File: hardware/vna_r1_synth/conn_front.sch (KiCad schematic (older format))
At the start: 5 parts

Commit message: work on vna r1 synth schematic
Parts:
- added C? (x5): C_Small, symbol C_Small
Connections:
- net AUX_OUT: now also C?.2; no longer U?.1 (RF)
- net LO_1: now also C?.2; no longer U?.1 (RF)
- net LO_2: now also C?.2; no longer U?.1 (RF)
- net PORT_1: now also C?.2; no longer U?.1 (RF)
- net PORT_2: now also C?.2; no longer U?.1 (RF)
- new net: C?.1, U?.1 (RF) (x5)
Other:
- note removed: "PORTS 1 and 2 are DC coupled to 0V"
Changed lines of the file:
@@
 Comment4 ""
 $EndDescr
-Text HLabel 5450 1600 0    60   Input ~ 0
+Text HLabel 4900 1600 0    60   Input ~ 0
 PORT_1
-Text HLabel 5450 2700 0    60   Input ~ 0
+Text HLabel 4900 2700 0    60   Input ~ 0
 PORT_2
-Text HLabel 5500 4100 0    60   Input ~ 0
+Text HLabel 4950 4100 0    60   Input ~ 0
 LO_1
-Text HLabel 5500 6500 0    60   Input ~ 0
+Text HLabel 4950 6500 0    60   Input ~ 0
 LO_2
-Text HLabel 5500 5200 0    60   Input ~ 0
+Text HLabel 4950 5200 0    60   Input ~ 0
 AUX_OUT
 $Comp
@@
 	1    0    0    -1
 $EndComp
-Wire Wire Line
-	6000 2050 6000 2100
-Wire Wire Line
-	6000 2100 6100 2100
-Wire Wire Line
-	6100 2100 6100 2050
-Wire Wire Line
-	6050 2100 6050 2150
-Connection ~ 6050 2100
-Wire Wire Line
-	5450 1600 5650 1600
 $Comp
 L CONN_SMA_2GND U?
@@
 	1    0    0    -1
 $EndComp
-Wire Wire Line
-	6000 3150 6000 3200
-Wire Wire Line
-	6000 3200 6100 3200
-Wire Wire Line
-	6100 3200 6100 3150
-Wire Wire Line
-	6050 3200 6050 3250
-Connection ~ 6050 3200
-Wire Wire Line
-	5450 2700 5650 2700
 $Comp
 L CONN_SMA_2GND U?
@@
 	1    0    0    -1
 $EndComp
-Wire Wire Line
-	6050 4550 6050 4600
-Wire Wire Line
-	6050 4600 6150 4600
-Wire Wire Line
-	6150 4600 6150 4550
-Wire Wire Line
-	6100 4600 6100 4650
-Connection ~ 6100 4600
-Wire Wire Line
-	5500 4100 5700 4100
 $Comp
 L CONN_SMA_2GND U?
@@
 	1    0    0    -1
 $EndComp
-Wire Wire Line
-	6050 5650 6050 5700
-Wire Wire Line
-	6050 5700 6150 5700
-Wire Wire Line
-	6150 5700 6150 5650
-Wire Wire Line
-	6100 5700 6100 5750
-Connection ~ 6100 5700
-Wire Wire Line
-	5500 5200 5700 5200
 $Comp
 L CONN_SMA_2GND U?
@@
 	1    0    0    -1
 $EndComp
+$Comp
+L C_Small C?
+U 1 1 5AC32053
+P 5200 4100
+F 0 "C?" H 5210 4170 50  0000 L CNN
+F 1 "C_Small" H 5210 4020 50  0000 L CNN
+F 2 "" H 5200 4100 50  0001 C CNN
+F 3 "" H 5200 4100 50  0001 C CNN
+	1    5200 4100
+	0    1    1    0
+$EndComp
+$Comp
+L C_Small C?
+U 1 1 5AC32137
+P 5200 5200
+F 0 "C?" H 5210 5270 50  0000 L CNN
+F 1 "C_Small" H 5210 5120 50  0000 L CNN
+F 2 "" H 5200 5200 50  0001 C CNN
+F 3 "" H 5200 5200 50  0001 C CNN
+	1    5200 5200
+	0    1    1    0
+$EndComp
+$Comp
+L C_Small C?
+U 1 1 5AC32269
+P 5200 6500
+F 0 "C?" H 5210 6570 50  0000 L CNN
+F 1 "C_Small" H 5210 6420 50  0000 L CNN
+F 2 "" H 5200 6500 50  0001 C CNN
+F 3 "" H 5200 6500 50  0001 C CNN
+	1    5200 6500
+	0    1    1    0
+$EndComp
+Wire Wire Line
+	6000 2050 6000 2100
+Wire Wire Line
+	6000 2100 6100 2100
+Wire Wire Line
+	6100 2100 6100 2050
+Wire Wire Line
+	6050 2100 6050 2150
+Connection ~ 6050 2100
+Wire Wire Line
+	5300 1600 5650 1600
+Wire Wire Line
+	6000 3150 6000 3200
+Wire Wire Line
+	6000 3200 6100 3200
+Wire Wire Line
+	6100 3200 6100 3150
+Wire Wire Line
+	6050 3200 6050 3250
+Connection ~ 6050 3200
+Wire Wire Line
+	5300 2700 5650 2700
+Wire Wire Line
+	6050 4550 6050 4600
+Wire Wire Line
+	6050 4600 6150 4600
+Wire Wire Line
+	6150 4600 6150 4550
+Wire Wire Line
+	6100 4600 6100 4650
+Connection ~ 6100 4600
+Wire Wire Line
+	5300 4100 5700 4100
+Wire Wire Line
+	6050 5650 6050 5700
+Wire Wire Line
+	6050 5700 6150 5700
+Wire Wire Line
+	6150 5700 6150 5650
+Wire Wire Line
+	6100 5700 6100 5750
+Connection ~ 6100 5700
+Wire Wire Line
+	5300 5200 5700 5200
 Wire Wire Line
 	6050 6950 6050 7000
@@
 Connection ~ 6100 7000
 Wire Wire Line
-	5500 6500 5700 6500
-Text Notes 4700 1100 0    60   ~ 0
-PORTS 1 and 2 are DC coupled to 0V
+	5300 6500 5700 6500
+Wire Wire Line
+	4900 1600 5100 1600
+Wire Wire Line
+	5100 2700 4900 2700
+Wire Wire Line
+	4950 4100 5100 4100
+Wire Wire Line
+	5100 5200 4950 5200
+Wire Wire Line
+	5100 6500 4950 6500
+$Comp
+L C_Small C?
+U 1 1 5AC31626
+P 5200 2700
+F 0 "C?" H 5210 2770 50  0000 L CNN
+F 1 "C_Small" H 5210 2620 50  0000 L CNN
+F 2 "" H 5200 2700 50  0001 C CNN
+F 3 "" H 5200 2700 50  0001 C CNN
+	1    5200 2700
+	0    1    1    0
+$EndComp
+$Comp
+L C_Small C?
+U 1 1 5AC31536
+P 5200 1600
+F 0 "C?" H 5210 1670 50  0000 L CNN
+F 1 "C_Small" H 5210 1520 50  0000 L CNN
+F 2 "" H 5200 1600 50  0001 C CNN
+F 3 "" H 5200 1600 50  0001 C CNN
+	1    5200 1600
+	0    1    1    0
+$EndComp
 $EndSCHEMATC

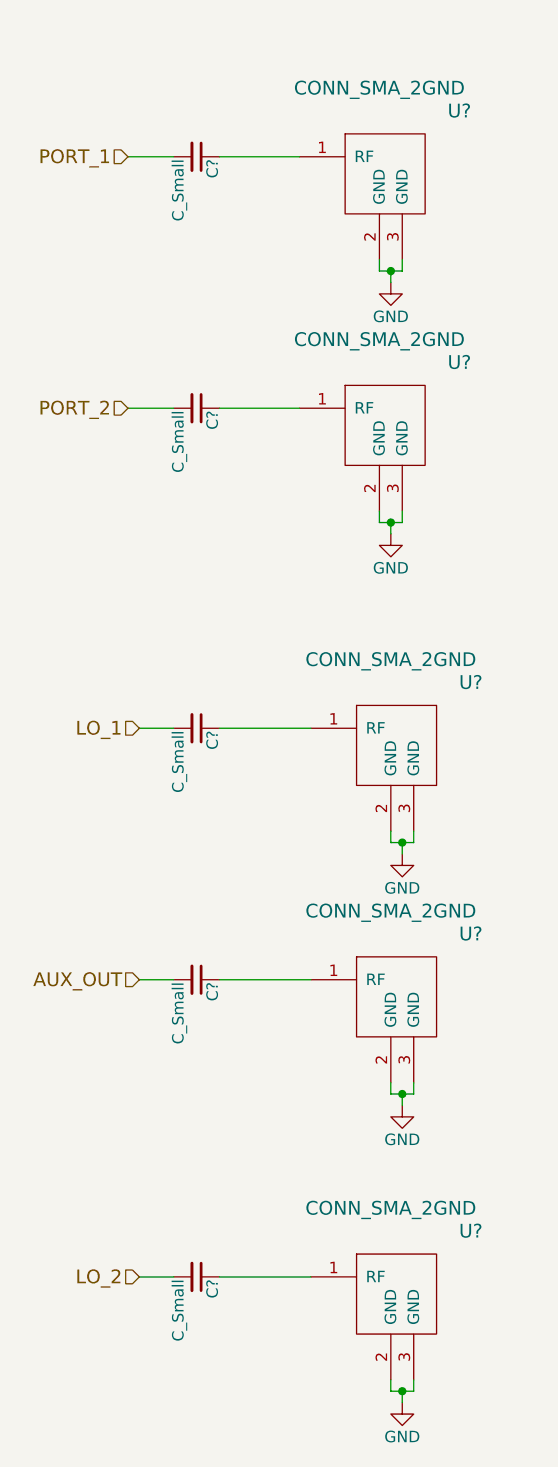
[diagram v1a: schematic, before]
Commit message: footprint assignment for vna r1 synth and demod
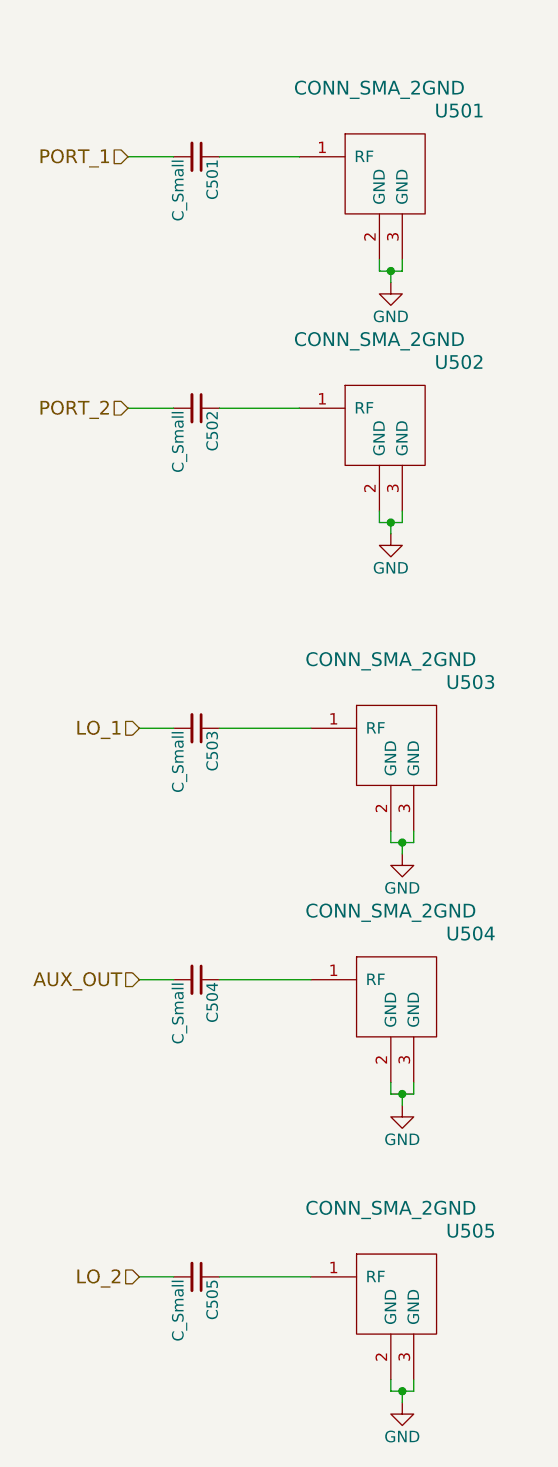
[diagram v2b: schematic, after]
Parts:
- C501, C502, C503, C504, C505: renamed from C?; footprint (none) -> Capacitors_SMD:C_0201
- U501, U502, U503, U504, U505: renamed from U?; footprint (none) -> vna_footprints:SMA_901-10512_6p7MIL_FR408_CPW_LAUNCH
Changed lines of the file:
@@
 AUX_OUT
 $Comp
-L CONN_SMA_2GND U?
+L CONN_SMA_2GND U501
 U 1 1 5AB94261
 P 6050 1600
-F 0 "U?" H 5750 1800 60  0000 C CNN
+F 0 "U501" H 5750 1800 60  0000 C CNN
 F 1 "CONN_SMA_2GND" H 6100 1900 60  0000 C CNN
-F 2 "" H 6050 1600 60  0000 C CNN
+F 2 "vna_footprints:SMA_901-10512_6p7MIL_FR408_CPW_LAUNCH" H 6050 1600 60  0001 C CNN
 F 3 "" H 6050 1600 60  0000 C CNN
 	1    6050 1600
@@
 $EndComp
 $Comp
-L GND #PWR?
+L GND #PWR0109
 U 1 1 5AB94285
 P 6050 2150
-F 0 "#PWR?" H 6050 1900 50  0001 C CNN
+F 0 "#PWR0109" H 6050 1900 50  0001 C CNN
 F 1 "GND" H 6050 2000 50  0000 C CNN
 F 2 "" H 6050 2150 50  0001 C CNN
@@
 $EndComp
 $Comp
-L CONN_SMA_2GND U?
+L CONN_SMA_2GND U502
 U 1 1 5ABBB801
 P 6050 2700
-F 0 "U?" H 5750 2900 60  0000 C CNN
+F 0 "U502" H 5750 2900 60  0000 C CNN
 F 1 "CONN_SMA_2GND" H 6100 3000 60  0000 C CNN
-F 2 "" H 6050 2700 60  0000 C CNN
+F 2 "vna_footprints:SMA_901-10512_6p7MIL_FR408_CPW_LAUNCH" H 6050 2700 60  0001 C CNN
 F 3 "" H 6050 2700 60  0000 C CNN
 	1    6050 2700
@@
 $EndComp
 $Comp
-L GND #PWR?
+L GND #PWR0110
 U 1 1 5ABBB807
 P 6050 3250
-F 0 "#PWR?" H 6050 3000 50  0001 C CNN
+F 0 "#PWR0110" H 6050 3000 50  0001 C CNN
 F 1 "GND" H 6050 3100 50  0000 C CNN
 F 2 "" H 6050 3250 50  0001 C CNN
@@
 $EndComp
 $Comp
-L CONN_SMA_2GND U?
+L CONN_SMA_2GND U503
 U 1 1 5ABBB8EC
 P 6100 4100
-F 0 "U?" H 5800 4300 60  0000 C CNN
+F 0 "U503" H 5800 4300 60  0000 C CNN
 F 1 "CONN_SMA_2GND" H 6150 4400 60  0000 C CNN
-F 2 "" H 6100 4100 60  0000 C CNN
+F 2 "vna_footprints:SMA_901-10512_6p7MIL_FR408_CPW_LAUNCH" H 6100 4100 60  0001 C CNN
 F 3 "" H 6100 4100 60  0000 C CNN
 	1    6100 4100
@@
 $EndComp
 $Comp
-L GND #PWR?
+L GND #PWR0111
 U 1 1 5ABBB8F2
 P 6100 4650
-F 0 "#PWR?" H 6100 4400 50  0001 C CNN
+F 0 "#PWR0111" H 6100 4400 50  0001 C CNN
 F 1 "GND" H 6100 4500 50  0000 C CNN
 F 2 "" H 6100 4650 50  0001 C CNN
@@
 $EndComp
 $Comp
-L CONN_SMA_2GND U?
+L CONN_SMA_2GND U504
 U 1 1 5ABBB8FF
 P 6100 5200
-F 0 "U?" H 5800 5400 60  0000 C CNN
+F 0 "U504" H 5800 5400 60  0000 C CNN
 F 1 "CONN_SMA_2GND" H 6150 5500 60  0000 C CNN
-F 2 "" H 6100 5200 60  0000 C CNN
+F 2 "vna_footprints:SMA_901-10512_6p7MIL_FR408_CPW_LAUNCH" H 6100 5200 60  0001 C CNN
 F 3 "" H 6100 5200 60  0000 C CNN
 	1    6100 5200
@@
 $EndComp
 $Comp
-L GND #PWR?
+L GND #PWR0112
 U 1 1 5ABBB905
 P 6100 5750
-F 0 "#PWR?" H 6100 5500 50  0001 C CNN
+F 0 "#PWR0112" H 6100 5500 50  0001 C CNN
 F 1 "GND" H 6100 5600 50  0000 C CNN
 F 2 "" H 6100 5750 50  0001 C CNN
@@
 $EndComp
 $Comp
-L CONN_SMA_2GND U?
+L CONN_SMA_2GND U505
 U 1 1 5ABBBAAA
 P 6100 6500
-F 0 "U?" H 5800 6700 60  0000 C CNN
+F 0 "U505" H 5800 6700 60  0000 C CNN
 F 1 "CONN_SMA_2GND" H 6150 6800 60  0000 C CNN
-F 2 "" H 6100 6500 60  0000 C CNN
+F 2 "vna_footprints:SMA_901-10512_6p7MIL_FR408_CPW_LAUNCH" H 6100 6500 60  0001 C CNN
 F 3 "" H 6100 6500 60  0000 C CNN
 	1    6100 6500
@@
 $EndComp
 $Comp
-L GND #PWR?
+L GND #PWR0113
 U 1 1 5ABBBAB0
 P 6100 7050
-F 0 "#PWR?" H 6100 6800 50  0001 C CNN
+F 0 "#PWR0113" H 6100 6800 50  0001 C CNN
 F 1 "GND" H 6100 6900 50  0000 C CNN
 F 2 "" H 6100 7050 50  0001 C CNN
@@
 $EndComp
 $Comp
-L C_Small C?
+L C_Small C503
 U 1 1 5AC32053
 P 5200 4100
-F 0 "C?" H 5210 4170 50  0000 L CNN
+F 0 "C503" H 5210 4170 50  0000 L CNN
 F 1 "C_Small" H 5210 4020 50  0000 L CNN
-F 2 "" H 5200 4100 50  0001 C CNN
+F 2 "Capacitors_SMD:C_0201" H 5200 4100 50  0001 C CNN
 F 3 "" H 5200 4100 50  0001 C CNN
 	1    5200 4100
@@
 $EndComp
 $Comp
-L C_Small C?
+L C_Small C504
 U 1 1 5AC32137
 P 5200 5200
-F 0 "C?" H 5210 5270 50  0000 L CNN
+F 0 "C504" H 5210 5270 50  0000 L CNN
 F 1 "C_Small" H 5210 5120 50  0000 L CNN
-F 2 "" H 5200 5200 50  0001 C CNN
+F 2 "Capacitors_SMD:C_0201" H 5200 5200 50  0001 C CNN
 F 3 "" H 5200 5200 50  0001 C CNN
 	1    5200 5200
@@
 $EndComp
 $Comp
-L C_Small C?
+L C_Small C505
 U 1 1 5AC32269
 P 5200 6500
-F 0 "C?" H 5210 6570 50  0000 L CNN
+F 0 "C505" H 5210 6570 50  0000 L CNN
 F 1 "C_Small" H 5210 6420 50  0000 L CNN
-F 2 "" H 5200 6500 50  0001 C CNN
+F 2 "Capacitors_SMD:C_0201" H 5200 6500 50  0001 C CNN
 F 3 "" H 5200 6500 50  0001 C CNN
 	1    5200 6500
@@
 	5100 6500 4950 6500
 $Comp
-L C_Small C?
+L C_Small C502
 U 1 1 5AC31626
 P 5200 2700
-F 0 "C?" H 5210 2770 50  0000 L CNN
+F 0 "C502" H 5210 2770 50  0000 L CNN
 F 1 "C_Small" H 5210 2620 50  0000 L CNN
-F 2 "" H 5200 2700 50  0001 C CNN
+F 2 "Capacitors_SMD:C_0201" H 5200 2700 50  0001 C CNN
 F 3 "" H 5200 2700 50  0001 C CNN
 	1    5200 2700
@@
 $EndComp
 $Comp
-L C_Small C?
+L C_Small C501
 U 1 1 5AC31536
 P 5200 1600
-F 0 "C?" H 5210 1670 50  0000 L CNN
+F 0 "C501" H 5210 1670 50  0000 L CNN
 F 1 "C_Small" H 5210 1520 50  0000 L CNN
-F 2 "" H 5200 1600 50  0001 C CNN
+F 2 "Capacitors_SMD:C_0201" H 5200 1600 50  0001 C CNN
 F 3 "" H 5200 1600 50  0001 C CNN
 	1    5200 1600

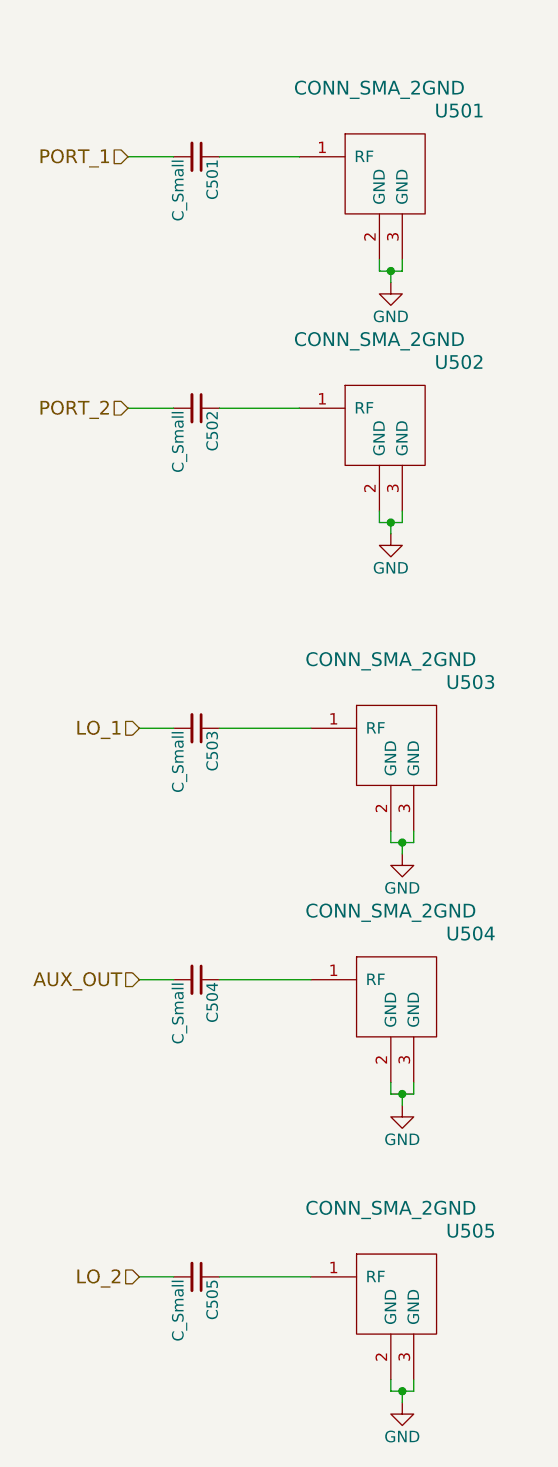
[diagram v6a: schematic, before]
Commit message: added missing schematic values
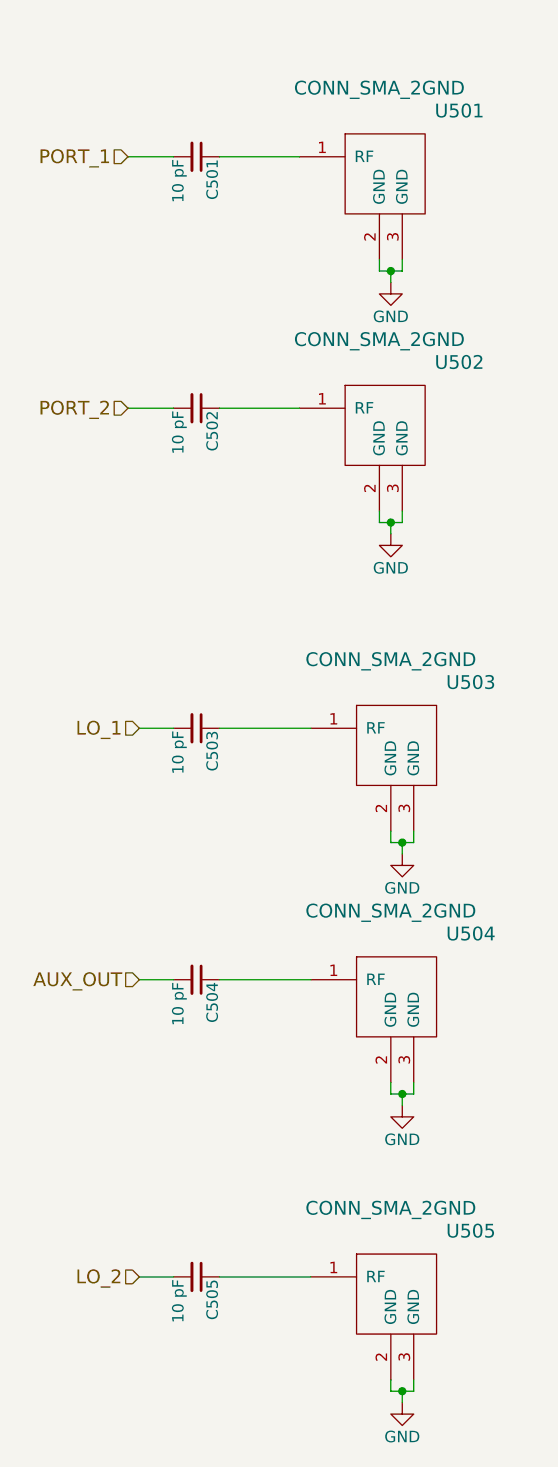
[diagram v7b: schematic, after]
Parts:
- C501, C502, C503, C504, C505: value C_Small -> 10 pF
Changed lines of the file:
@@
 P 5200 4100
 F 0 "C503" H 5210 4170 50  0000 L CNN
-F 1 "C_Small" H 5210 4020 50  0000 L CNN
+F 1 "10 pF" H 5210 4020 50  0000 L CNN
 F 2 "Capacitors_SMD:C_0201" H 5200 4100 50  0001 C CNN
 F 3 "" H 5200 4100 50  0001 C CNN
@@
 P 5200 5200
 F 0 "C504" H 5210 5270 50  0000 L CNN
-F 1 "C_Small" H 5210 5120 50  0000 L CNN
+F 1 "10 pF" H 5210 5120 50  0000 L CNN
 F 2 "Capacitors_SMD:C_0201" H 5200 5200 50  0001 C CNN
 F 3 "" H 5200 5200 50  0001 C CNN
@@
 P 5200 6500
 F 0 "C505" H 5210 6570 50  0000 L CNN
-F 1 "C_Small" H 5210 6420 50  0000 L CNN
+F 1 "10 pF" H 5210 6420 50  0000 L CNN
 F 2 "Capacitors_SMD:C_0201" H 5200 6500 50  0001 C CNN
 F 3 "" H 5200 6500 50  0001 C CNN
@@
 P 5200 2700
 F 0 "C502" H 5210 2770 50  0000 L CNN
-F 1 "C_Small" H 5210 2620 50  0000 L CNN
+F 1 "10 pF" H 5210 2620 50  0000 L CNN
 F 2 "Capacitors_SMD:C_0201" H 5200 2700 50  0001 C CNN
 F 3 "" H 5200 2700 50  0001 C CNN
@@
 P 5200 1600
 F 0 "C501" H 5210 1670 50  0000 L CNN
-F 1 "C_Small" H 5210 1520 50  0000 L CNN
+F 1 "10 pF" H 5210 1520 50  0000 L CNN
 F 2 "Capacitors_SMD:C_0201" H 5200 1600 50  0001 C CNN
 F 3 "" H 5200 1600 50  0001 C CNN

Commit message: bypass if filter in vna r1 demod
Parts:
- C501, C502, C503, C504, C505: symbol C_Small -> device:C_Small
- U501, U502, U503, U504, U505: symbol CONN_SMA_2GND -> conn_sma_2gnd:CONN_SMA_2GND
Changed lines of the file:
@@
-EESchema Schematic File Version 2
-LIBS:power
-LIBS:device
-LIBS:switches
-LIBS:relays
-LIBS:motors
-LIBS:transistors
-LIBS:conn
-LIBS:linear
-LIBS:regul
-LIBS:74xx
-LIBS:cmos4000
-LIBS:adc-dac
-LIBS:memory
-LIBS:xilinx
-LIBS:microcontrollers
-LIBS:dsp
-LIBS:microchip
-LIBS:analog_switches
-LIBS:motorola
-LIBS:texas
-LIBS:intel
-LIBS:audio
-LIBS:interface
-LIBS:digital-audio
-LIBS:philips
-LIBS:display
-LIBS:cypress
-LIBS:siliconi
-LIBS:opto
-LIBS:atmel
-LIBS:contrib
-LIBS:valves
-LIBS:adrf5020
-LIBS:tps2051
-LIBS:resistive_bridge
-LIBS:lm2776
-LIBS:max810
-LIBS:vdd_clk
-LIBS:vdd_lo
-LIBS:vdd_rf
-LIBS:lan8710a
-LIBS:ad9577
-LIBS:okr_t3-w12-c
-LIBS:adp7158
-LIBS:maam-011100
-LIBS:ltc2054cs5
-LIBS:ltc2630
-LIBS:trf37b73
-LIBS:nc7wzu04
-LIBS:adrf5040
-LIBS:lmx2594
-LIBS:tps255xx
-LIBS:tps2065d
-LIBS:masw-008322-tr1000
-LIBS:max510
-LIBS:pe42541
-LIBS:txco
-LIBS:tps793
-LIBS:tpd4s012
-LIBS:tcm-63ax+
-LIBS:sn74lvc1g07
-LIBS:scbd-16-63
-LIBS:rf_crossbar
-LIBS:pwr_splitter
-LIBS:pe43705
-LIBS:pe42540
-LIBS:pe42521
-LIBS:pcm2900
-LIBS:nc7sv74kbx
-LIBS:nb3n551
-LIBS:mounting_hole
-LIBS:mounting_box
-LIBS:mga-82563
-LIBS:max2605
-LIBS:maam-011101
-LIBS:ltc5596
-LIBS:ltc5549
-LIBS:ltc2323
-LIBS:ltc1983
-LIBS:ltc1566-1
-LIBS:lt1819
-LIBS:lt1567
-LIBS:lmx2592
-LIBS:lmk61e2
-LIBS:hmc629
-LIBS:hmc525
-LIBS:hmc475
-LIBS:hmc424
-LIBS:hmc321
-LIBS:hmc311sc70
-LIBS:conn_sma_2gnd
-LIBS:conn_sma
-LIBS:conn_microsd
-LIBS:cmm0511-qt-0g0t
-LIBS:cat102
-LIBS:boosterpack_ti
-LIBS:ammp-6120
-LIBS:adm7150
-LIBS:adl5902
-LIBS:adl5380
-LIBS:adf4355-3
-LIBS:ad9864
-LIBS:75451
-LIBS:74xx1g14
-LIBS:74hc04_full
-LIBS:74hc04
-LIBS:lm27762
-LIBS:74lvc1g00
-LIBS:74lvc1g32
-LIBS:ld39100
+EESchema Schematic File Version 4
 LIBS:vna_r1_synth-cache
-EELAYER 25 0
+EELAYER 26 0
 EELAYER END
 $Descr A4 11693 8268
@@
 AUX_OUT
 $Comp
-L CONN_SMA_2GND U501
+L conn_sma_2gnd:CONN_SMA_2GND U501
 U 1 1 5AB94261
 P 6050 1600
@@
 $EndComp
 $Comp
-L GND #PWR077
+L power:GND #PWR077
 U 1 1 5AB94285
 P 6050 2150
@@
 $EndComp
 $Comp
-L CONN_SMA_2GND U502
+L conn_sma_2gnd:CONN_SMA_2GND U502
 U 1 1 5ABBB801
 P 6050 2700
@@
 $EndComp
 $Comp
-L GND #PWR078
+L power:GND #PWR078
 U 1 1 5ABBB807
 P 6050 3250
@@
 $EndComp
 $Comp
-L CONN_SMA_2GND U503
+L conn_sma_2gnd:CONN_SMA_2GND U503
 U 1 1 5ABBB8EC
 P 6100 4100
@@
 $EndComp
 $Comp
-L GND #PWR079
+L power:GND #PWR079
 U 1 1 5ABBB8F2
 P 6100 4650
@@
 $EndComp
 $Comp
-L CONN_SMA_2GND U504
+L conn_sma_2gnd:CONN_SMA_2GND U504
 U 1 1 5ABBB8FF
 P 6100 5200
@@
 $EndComp
 $Comp
-L GND #PWR080
+L power:GND #PWR080
 U 1 1 5ABBB905
 P 6100 5750
@@
 $EndComp
 $Comp
-L CONN_SMA_2GND U505
+L conn_sma_2gnd:CONN_SMA_2GND U505
 U 1 1 5ABBBAAA
 P 6100 6500
@@
 $EndComp
 $Comp
-L GND #PWR081
+L power:GND #PWR081
 U 1 1 5ABBBAB0
 P 6100 7050
@@
 $EndComp
 $Comp
-L C_Small C503
+L device:C_Small C503
 U 1 1 5AC32053
 P 5200 4100
@@
 $EndComp
 $Comp
-L C_Small C504
+L device:C_Small C504
 U 1 1 5AC32137
 P 5200 5200
@@
 $EndComp
 $Comp
-L C_Small C505
+L device:C_Small C505
 U 1 1 5AC32269
 P 5200 6500
@@
 	5100 6500 4950 6500
 $Comp
-L C_Small C502
+L device:C_Small C502
 U 1 1 5AC31626
 P 5200 2700
@@
 $EndComp
 $Comp
-L C_Small C501
+L device:C_Small C501
 U 1 1 5AC31536
 P 5200 1600
